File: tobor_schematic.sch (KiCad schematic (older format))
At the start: 19 parts

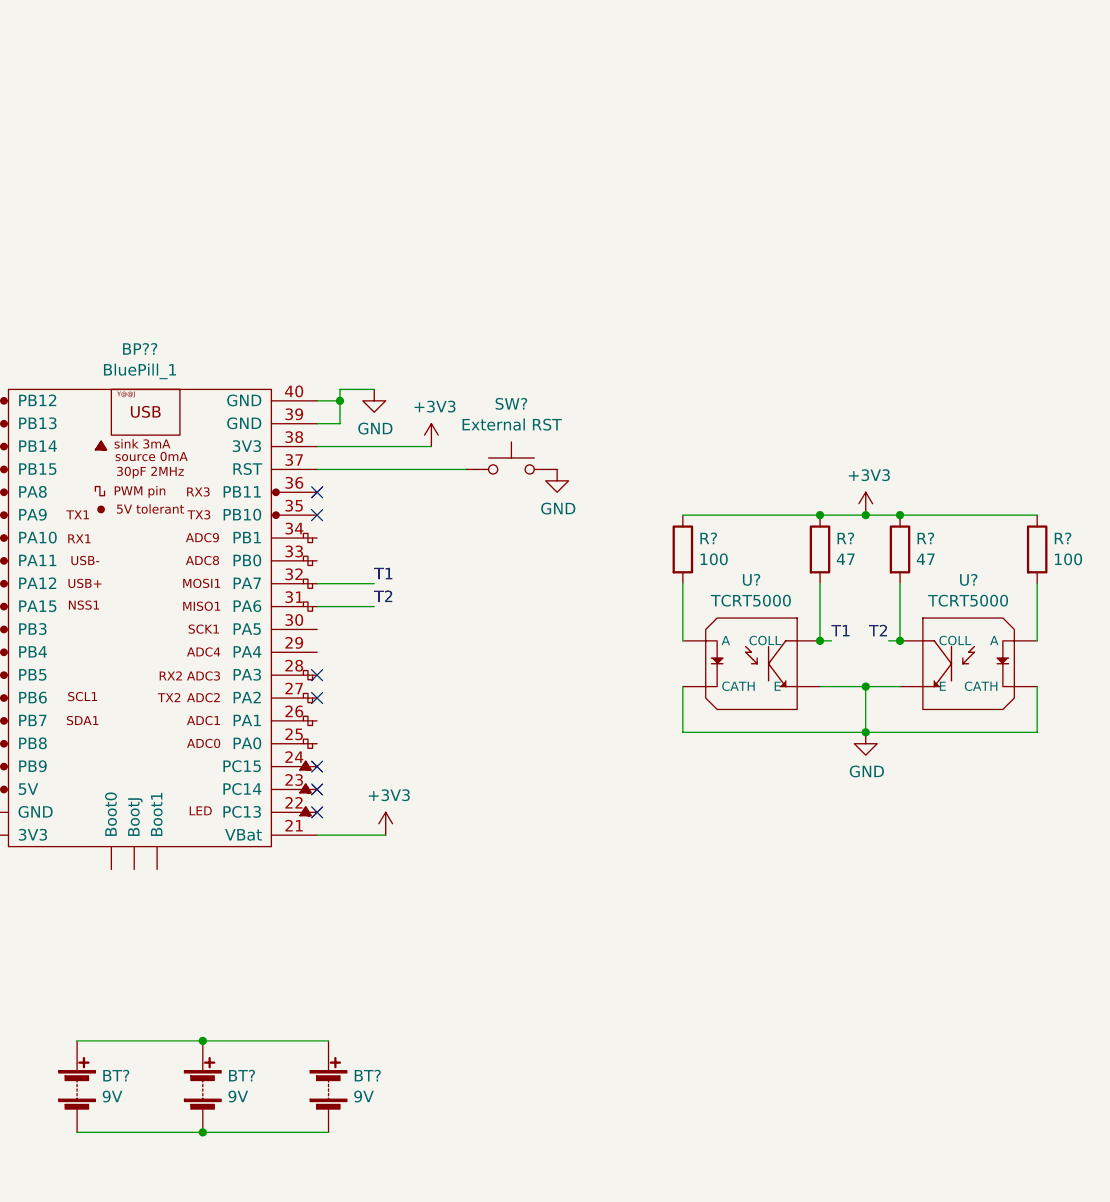
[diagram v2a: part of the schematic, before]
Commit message: Add H Bridges
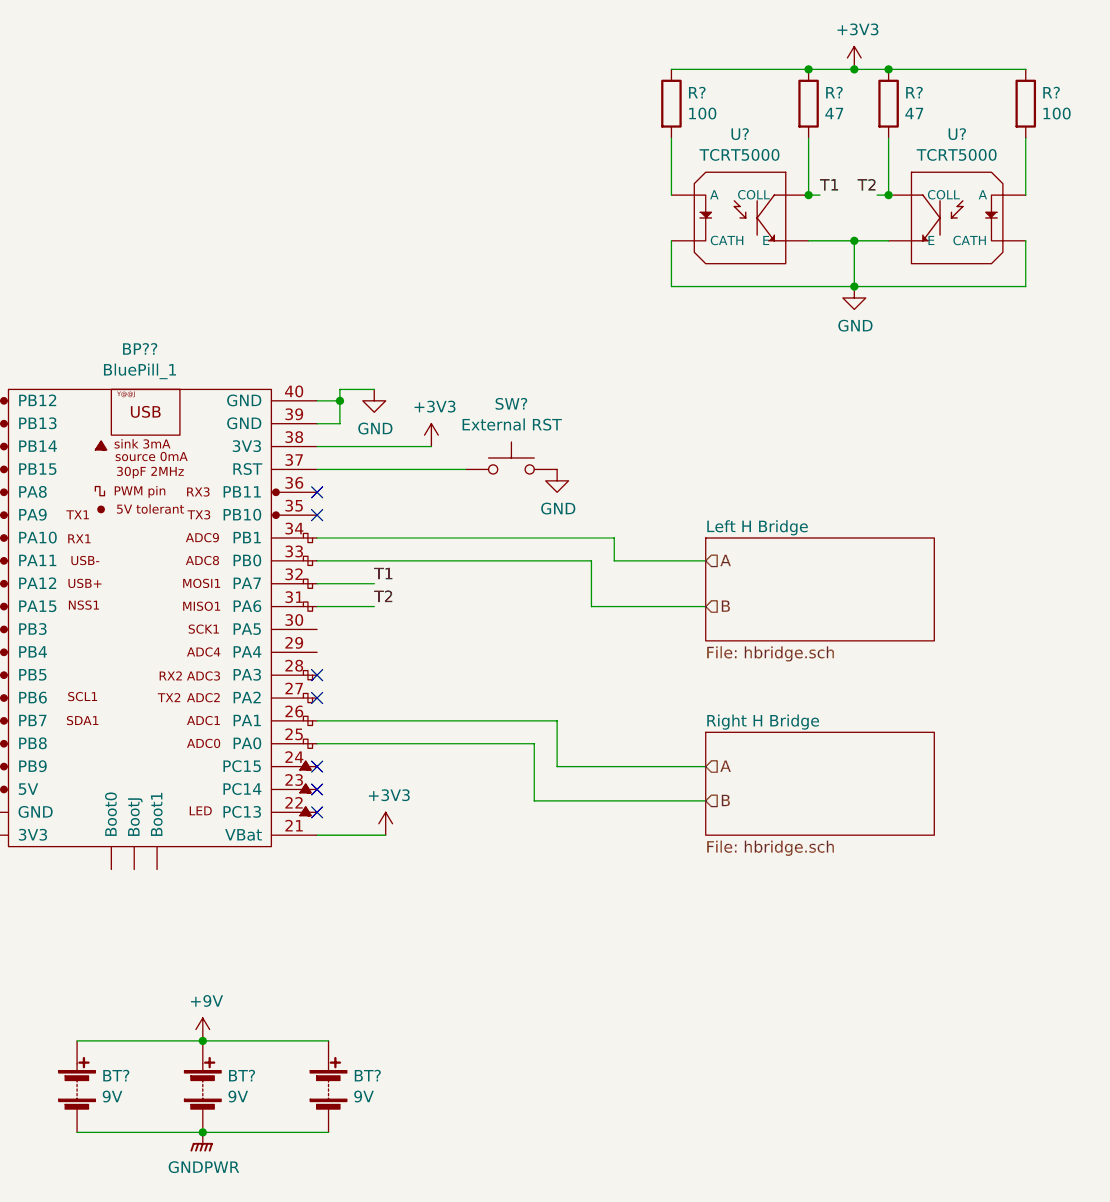
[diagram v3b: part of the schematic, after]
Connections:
- net B: now reaches BP??.25 (PA0)
- net B: now also BP??.33 (PB0)
- net A: now reaches BP??.26 (PA1)
- net A: now also BP??.34 (PB1)
- net +9V: now reaches BT?.1 (+), BT?.1 (+), BT?.1 (+)
- net GNDPWR: now reaches BT?.2 (-), BT?.2 (-), BT?.2 (-)
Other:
- moved on the sheet: R?, U?
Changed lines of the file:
@@
 $Descr A4 11693 8268
 encoding utf-8
-Sheet 1 1
+Sheet 1 3
 Title "Tobor"
 Date ""
@@
 Wire Wire Line
 	6750 4950 7050 4950
-$Comp
-L TCRT5000:TCRT5000 U?
-U 1 1 5EF5CF42
-P 8650 4200
-F 0 "U?" H 8650 4565 50  0000 C CNN
-F 1 "TCRT5000" H 8650 4474 50  0000 C CNN
-F 2 "OPTO_TCRT5000" H 8650 4200 50  0001 L BNN
-F 3 "Vishay" H 8650 4200 50  0001 L BNN
-F 4 "7.2mm" H 8650 4200 50  0001 L BNN "Field4"
-F 5 "Manufacturer recommendations" H 8650 4200 50  0001 L BNN "Field5"
-F 6 "1.7" H 8650 4200 50  0001 L BNN "Field6"
-	1    8650 4200
-	1    0    0    -1
-$EndComp
-$Comp
-L Device:R R?
-U 1 1 5EF5F265
-P 8350 3700
-F 0 "R?" H 8420 3746 50  0000 L CNN
-F 1 "100" H 8420 3655 50  0000 L CNN
-F 2 "" V 8280 3700 50  0001 C CNN
-F 3 "~" H 8350 3700 50  0001 C CNN
-	1    8350 3700
-	1    0    0    -1
-$EndComp
-$Comp
-L Device:R R?
-U 1 1 5EF5F885
-P 8950 3700
-F 0 "R?" H 9020 3746 50  0000 L CNN
-F 1 "47" H 9020 3655 50  0000 L CNN
-F 2 "" V 8880 3700 50  0001 C CNN
-F 3 "~" H 8950 3700 50  0001 C CNN
-	1    8950 3700
-	1    0    0    -1
-$EndComp
-Wire Wire Line
-	8350 3850 8350 4100
-Wire Wire Line
-	8950 3850 8950 4100
-$Comp
-L TCRT5000:TCRT5000 U?
-U 1 1 5EF643B0
-P 9600 4200
-F 0 "U?" H 9600 4565 50  0000 C CNN
-F 1 "TCRT5000" H 9600 4474 50  0000 C CNN
-F 2 "OPTO_TCRT5000" H 9600 4200 50  0001 L BNN
-F 3 "Vishay" H 9600 4200 50  0001 L BNN
-F 4 "7.2mm" H 9600 4200 50  0001 L BNN "Field4"
-F 5 "Manufacturer recommendations" H 9600 4200 50  0001 L BNN "Field5"
-F 6 "1.7" H 9600 4200 50  0001 L BNN "Field6"
-	1    9600 4200
-	-1   0    0    -1
-$EndComp
-$Comp
-L Device:R R?
-U 1 1 5EF65515
-P 9900 3700
-F 0 "R?" H 9970 3746 50  0000 L CNN
-F 1 "100" H 9970 3655 50  0000 L CNN
-F 2 "" V 9830 3700 50  0001 C CNN
-F 3 "~" H 9900 3700 50  0001 C CNN
-	1    9900 3700
-	1    0    0    -1
-$EndComp
-$Comp
-L Device:R R?
-U 1 1 5EF65A73
-P 9300 3700
-F 0 "R?" H 9370 3746 50  0000 L CNN
-F 1 "47" H 9370 3655 50  0000 L CNN
-F 2 "" V 9230 3700 50  0001 C CNN
-F 3 "~" H 9300 3700 50  0001 C CNN
-	1    9300 3700
-	1    0    0    -1
-$EndComp
-Wire Wire Line
-	9300 3850 9300 4100
-Wire Wire Line
-	9900 4100 9900 3850
-$Comp
-L power:+3V3 #PWR?
-U 1 1 5EF674E2
-P 9150 3550
-F 0 "#PWR?" H 9150 3400 50  0001 C CNN
-F 1 "+3V3" H 9165 3723 50  0000 C CNN
-F 2 "" H 9150 3550 50  0001 C CNN
-F 3 "" H 9150 3550 50  0001 C CNN
-	1    9150 3550
-	1    0    0    -1
-$EndComp
-Wire Wire Line
-	8350 3550 8950 3550
-Wire Wire Line
-	8950 3550 9150 3550
-Connection ~ 8950 3550
-Wire Wire Line
-	9150 3550 9300 3550
-Connection ~ 9150 3550
-Wire Wire Line
-	9300 3550 9900 3550
-Connection ~ 9300 3550
-$Comp
-L power:GND #PWR?
-U 1 1 5EF69FA1
-P 9150 4500
-F 0 "#PWR?" H 9150 4250 50  0001 C CNN
-F 1 "GND" H 9155 4327 50  0000 C CNN
-F 2 "" H 9150 4500 50  0001 C CNN
-F 3 "" H 9150 4500 50  0001 C CNN
-	1    9150 4500
-	1    0    0    -1
-$EndComp
-Wire Wire Line
-	9150 4500 9150 4300
-Wire Wire Line
-	9150 4300 8950 4300
-Wire Wire Line
-	9300 4300 9150 4300
-Connection ~ 9150 4300
-Wire Wire Line
-	8350 4300 8350 4500
-Wire Wire Line
-	8350 4500 9150 4500
-Connection ~ 9150 4500
-Wire Wire Line
-	9150 4500 9900 4500
-Wire Wire Line
-	9900 4500 9900 4300
 Text Label 7000 3850 0    50   ~ 0
 T1
 Text Label 7000 3950 0    50   ~ 0
-T2
-Wire Wire Line
-	8950 4100 9000 4100
-Connection ~ 8950 4100
-Text Label 9000 4100 0    50   ~ 0
-T1
-Wire Wire Line
-	9300 4100 9250 4100
-Connection ~ 9300 4100
-Text Label 9250 4100 2    50   ~ 0
 T2
 Wire Wire Line
@@
 Wire Wire Line
 	4200 3000 4200 2950
+$Comp
+L power:+9V #PWR?
+U 1 1 5EF6748E
+P 6250 5850
+F 0 "#PWR?" H 6250 5700 50  0001 C CNN
+F 1 "+9V" H 6265 6023 50  0000 C CNN
+F 2 "" H 6250 5850 50  0001 C CNN
+F 3 "" H 6250 5850 50  0001 C CNN
+	1    6250 5850
+	1    0    0    -1
+$EndComp
+$Comp
+L power:GNDPWR #PWR?
+U 1 1 5EF69A69
+P 6250 6250
+F 0 "#PWR?" H 6250 6050 50  0001 C CNN
+F 1 "GNDPWR" H 6254 6096 50  0000 C CNN
+F 2 "" H 6250 6200 50  0001 C CNN
+F 3 "" H 6250 6200 50  0001 C CNN
+	1    6250 6250
+	1    0    0    -1
+$EndComp
+Text Label 9200 2150 2    50   ~ 0
+T2
+Connection ~ 9250 2150
+Wire Wire Line
+	9250 2150 9200 2150
+Text Label 8950 2150 0    50   ~ 0
+T1
+Connection ~ 8900 2150
+Wire Wire Line
+	8900 2150 8950 2150
+Wire Wire Line
+	9850 2550 9850 2350
+Wire Wire Line
+	9100 2550 9850 2550
+Connection ~ 9100 2550
+Wire Wire Line
+	8300 2550 9100 2550
+Wire Wire Line
+	8300 2350 8300 2550
+Connection ~ 9100 2350
+Wire Wire Line
+	9250 2350 9100 2350
+Wire Wire Line
+	9100 2350 8900 2350
+Wire Wire Line
+	9100 2550 9100 2350
+$Comp
+L power:GND #PWR?
+U 1 1 5EF69FA1
+P 9100 2550
+F 0 "#PWR?" H 9100 2300 50  0001 C CNN
+F 1 "GND" H 9105 2377 50  0000 C CNN
+F 2 "" H 9100 2550 50  0001 C CNN
+F 3 "" H 9100 2550 50  0001 C CNN
+	1    9100 2550
+	1    0    0    -1
+$EndComp
+Connection ~ 9250 1600
+Wire Wire Line
+	9250 1600 9850 1600
+Connection ~ 9100 1600
+Wire Wire Line
+	9100 1600 9250 1600
+Connection ~ 8900 1600
+Wire Wire Line
+	8900 1600 9100 1600
+Wire Wire Line
+	8300 1600 8900 1600
+$Comp
+L power:+3V3 #PWR?
+U 1 1 5EF674E2
+P 9100 1600
+F 0 "#PWR?" H 9100 1450 50  0001 C CNN
+F 1 "+3V3" H 9115 1773 50  0000 C CNN
+F 2 "" H 9100 1600 50  0001 C CNN
+F 3 "" H 9100 1600 50  0001 C CNN
+	1    9100 1600
+	1    0    0    -1
+$EndComp
+Wire Wire Line
+	9850 2150 9850 1900
+Wire Wire Line
+	9250 1900 9250 2150
+$Comp
+L Device:R R?
+U 1 1 5EF65A73
+P 9250 1750
+F 0 "R?" H 9320 1796 50  0000 L CNN
+F 1 "47" H 9320 1705 50  0000 L CNN
+F 2 "" V 9180 1750 50  0001 C CNN
+F 3 "~" H 9250 1750 50  0001 C CNN
+	1    9250 1750
+	1    0    0    -1
+$EndComp
+$Comp
+L Device:R R?
+U 1 1 5EF65515
+P 9850 1750
+F 0 "R?" H 9920 1796 50  0000 L CNN
+F 1 "100" H 9920 1705 50  0000 L CNN
+F 2 "" V 9780 1750 50  0001 C CNN
+F 3 "~" H 9850 1750 50  0001 C CNN
+	1    9850 1750
+	1    0    0    -1
+$EndComp
+$Comp
+L TCRT5000:TCRT5000 U?
+U 1 1 5EF643B0
+P 9550 2250
+F 0 "U?" H 9550 2615 50  0000 C CNN
+F 1 "TCRT5000" H 9550 2524 50  0000 C CNN
+F 2 "OPTO_TCRT5000" H 9550 2250 50  0001 L BNN
+F 3 "Vishay" H 9550 2250 50  0001 L BNN
+F 4 "7.2mm" H 9550 2250 50  0001 L BNN "Field4"
+F 5 "Manufacturer recommendations" H 9550 2250 50  0001 L BNN "Field5"
+F 6 "1.7" H 9550 2250 50  0001 L BNN "Field6"
+	1    9550 2250
+	-1   0    0    -1
+$EndComp
+Wire Wire Line
+	8900 1900 8900 2150
+Wire Wire Line
+	8300 1900 8300 2150
+$Comp
+L Device:R R?
+U 1 1 5EF5F885
+P 8900 1750
+F 0 "R?" H 8970 1796 50  0000 L CNN
+F 1 "47" H 8970 1705 50  0000 L CNN
+F 2 "" V 8830 1750 50  0001 C CNN
+F 3 "~" H 8900 1750 50  0001 C CNN
+	1    8900 1750
+	1    0    0    -1
+$EndComp
+$Comp
+L Device:R R?
+U 1 1 5EF5F265
+P 8300 1750
+F 0 "R?" H 8370 1796 50  0000 L CNN
+F 1 "100" H 8370 1705 50  0000 L CNN
+F 2 "" V 8230 1750 50  0001 C CNN
+F 3 "~" H 8300 1750 50  0001 C CNN
+	1    8300 1750
+	1    0    0    -1
+$EndComp
+$Comp
+L TCRT5000:TCRT5000 U?
+U 1 1 5EF5CF42
+P 8600 2250
+F 0 "U?" H 8600 2615 50  0000 C CNN
+F 1 "TCRT5000" H 8600 2524 50  0000 C CNN
+F 2 "OPTO_TCRT5000" H 8600 2250 50  0001 L BNN
+F 3 "Vishay" H 8600 2250 50  0001 L BNN
+F 4 "7.2mm" H 8600 2250 50  0001 L BNN "Field4"
+F 5 "Manufacturer recommendations" H 8600 2250 50  0001 L BNN "Field5"
+F 6 "1.7" H 8600 2250 50  0001 L BNN "Field6"
+	1    8600 2250
+	1    0    0    -1
+$EndComp
+$Sheet
+S 8450 3650 1000 450
+U 5EFA9D4F
+F0 "Left H Bridge" 50
+F1 "hbridge.sch" 50
+$EndSheet
+Text HLabel 8450 3750 2    50   Input ~ 0
+A
+Text HLabel 8450 3950 2    50   Input ~ 0
+B
+Wire Wire Line
+	6750 3650 8050 3650
+Wire Wire Line
+	8050 3650 8050 3750
+Wire Wire Line
+	8050 3750 8450 3750
+Wire Wire Line
+	6750 3750 7950 3750
+Wire Wire Line
+	7950 3750 7950 3950
+Wire Wire Line
+	7950 3950 8450 3950
+$Sheet
+S 8450 4500 1000 450
+U 5F04487B
+F0 "Right H Bridge" 50
+F1 "hbridge.sch" 50
+$EndSheet
+Text HLabel 8450 4650 2    50   Input ~ 0
+A
+Text HLabel 8450 4800 2    50   Input ~ 0
+B
+Wire Wire Line
+	6750 4450 7800 4450
+Wire Wire Line
+	7800 4450 7800 4650
+Wire Wire Line
+	7800 4650 8450 4650
+Wire Wire Line
+	6750 4550 7700 4550
+Wire Wire Line
+	7700 4550 7700 4800
+Wire Wire Line
+	7700 4800 8450 4800
 $EndSCHEMATC

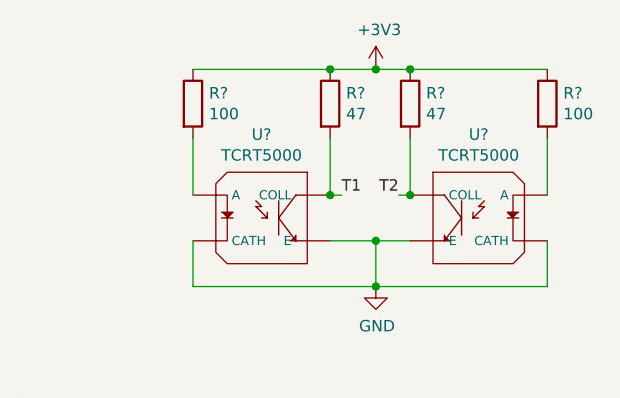
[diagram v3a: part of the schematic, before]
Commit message: Fix tape sensor resistor value
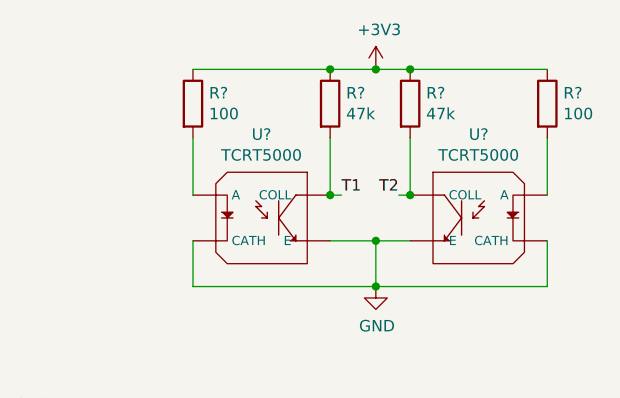
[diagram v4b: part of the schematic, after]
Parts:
- R? (x2): value 47 -> 47k
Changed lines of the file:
@@
 P 9250 1750
 F 0 "R?" H 9320 1796 50  0000 L CNN
-F 1 "47" H 9320 1705 50  0000 L CNN
+F 1 "47k" H 9320 1705 50  0000 L CNN
 F 2 "" V 9180 1750 50  0001 C CNN
 F 3 "~" H 9250 1750 50  0001 C CNN
@@
 P 8900 1750
 F 0 "R?" H 8970 1796 50  0000 L CNN
-F 1 "47" H 8970 1705 50  0000 L CNN
+F 1 "47k" H 8970 1705 50  0000 L CNN
 F 2 "" V 8830 1750 50  0001 C CNN
 F 3 "~" H 8900 1750 50  0001 C CNN
